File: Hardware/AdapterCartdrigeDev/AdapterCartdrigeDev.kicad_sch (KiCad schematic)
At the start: 3 parts, among them J1 ROM, U1 28C256

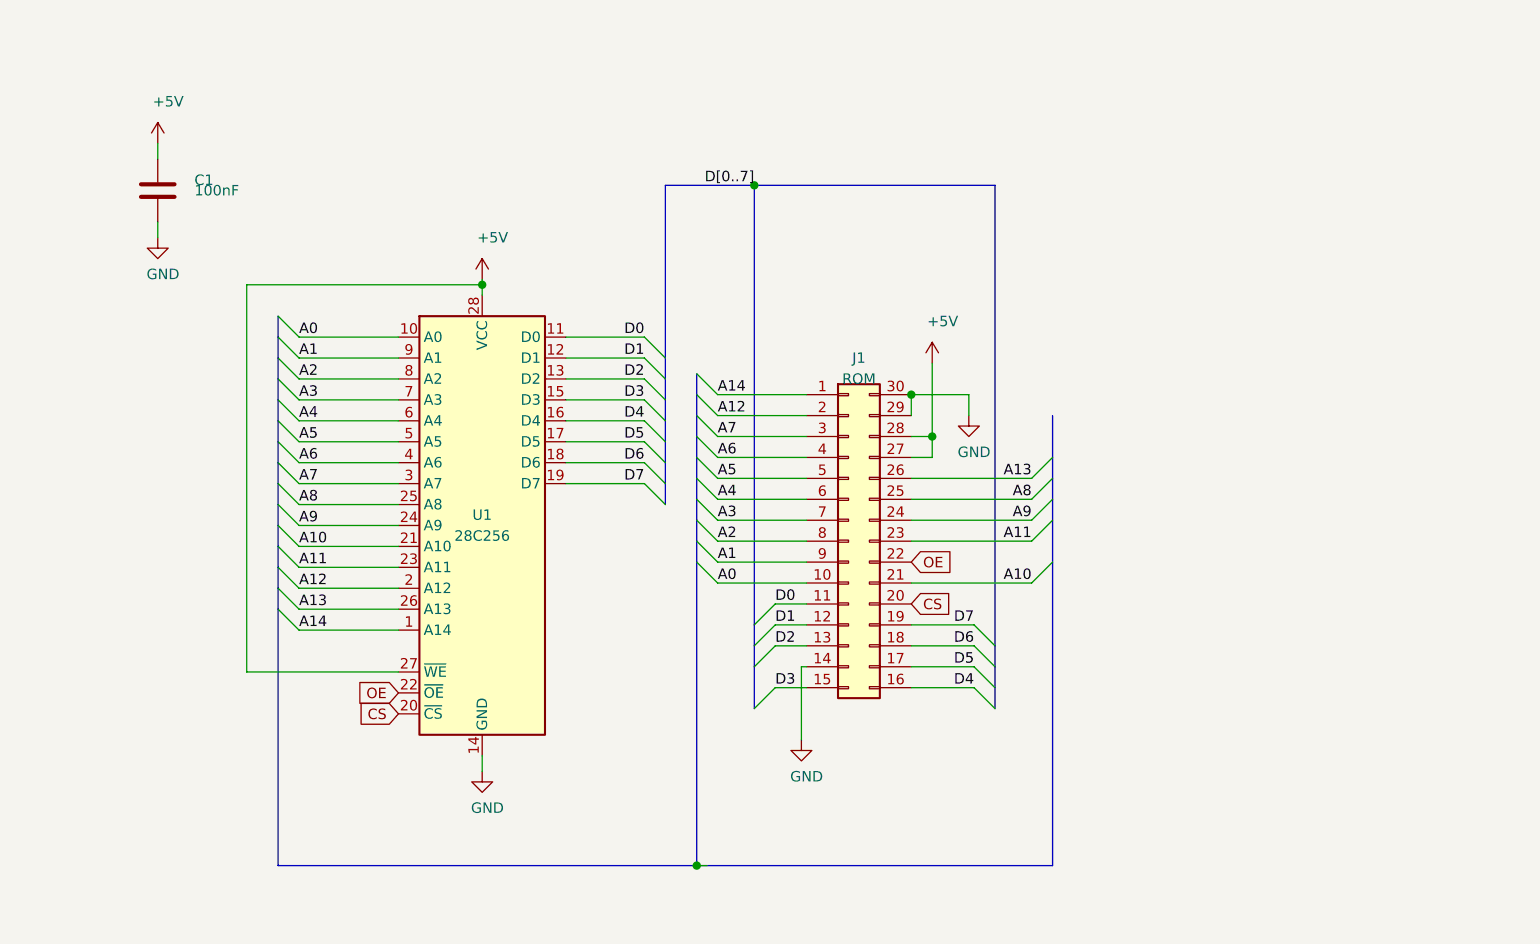
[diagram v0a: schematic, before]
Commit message: New PLD logic, VGA, DMA ...
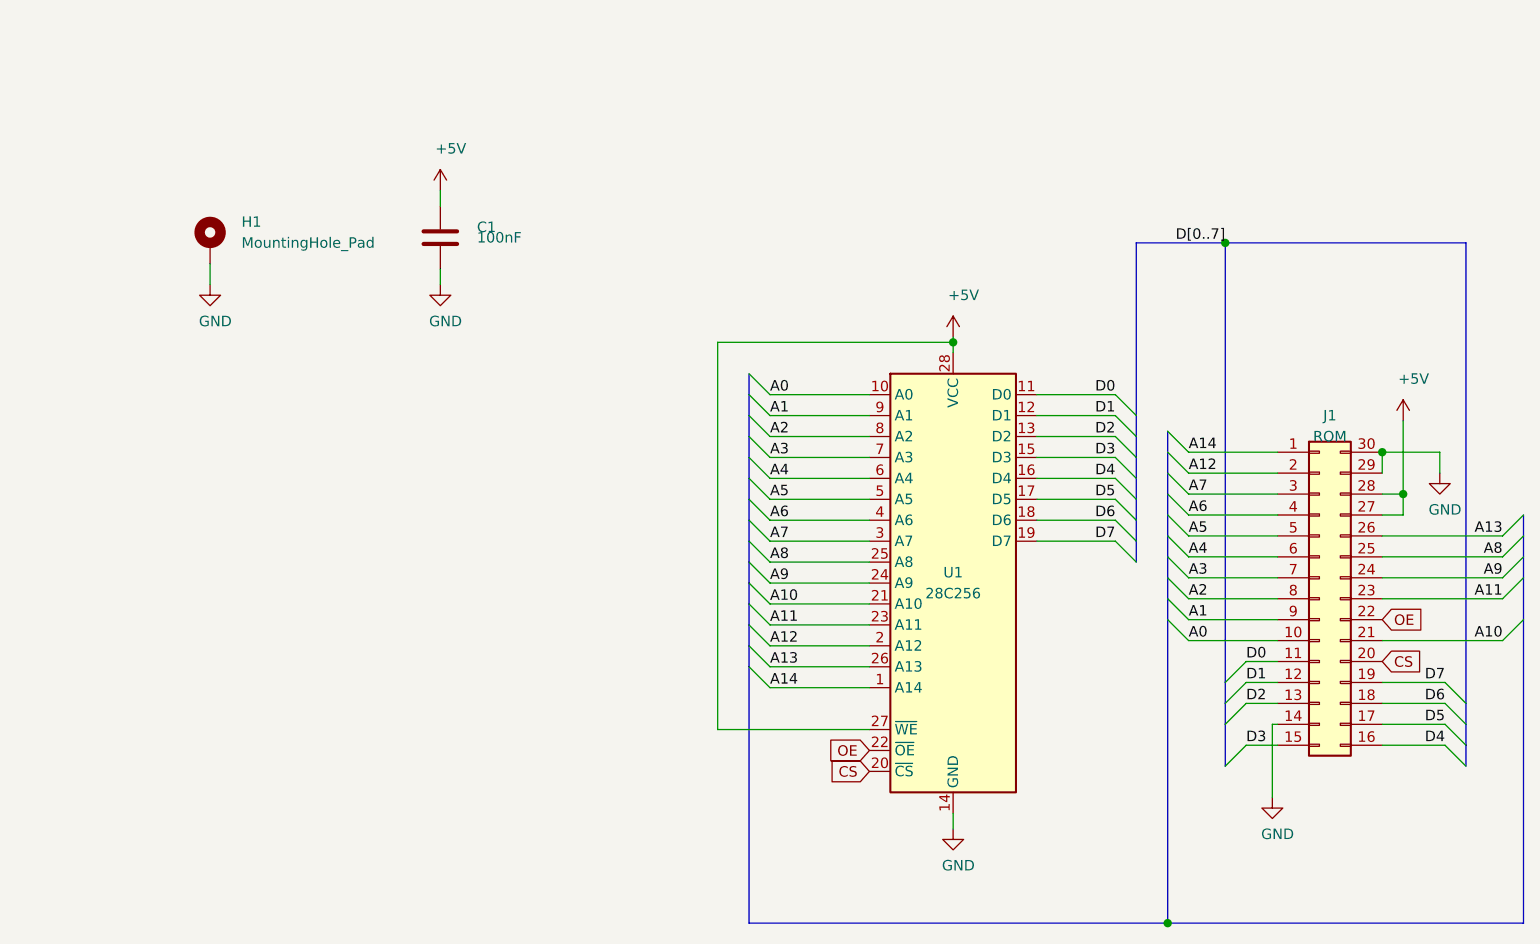
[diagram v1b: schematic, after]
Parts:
- added H1: MountingHole_Pad, MountingHole:MountingHole_3.2mm_M3, symbol Mechanical:MountingHole_Pad
- J1: footprint Connector_PinHeader_2.54mm:PinHeader_2x15_P2.54mm_Horizontal -> Connector_PinHeader_2.54mm:PinHeader_2x15_P2.54mm_Vertical
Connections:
- net GND: now also H1.1
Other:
- moved on the sheet: C1, J1, U1

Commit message: Fix
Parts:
- added H2, H3: MountingHole_Pad, MountingHole:MountingHole_3.2mm_M3, symbol Mechanical:MountingHole_Pad
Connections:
- net GND: now also H2.1, H3.1
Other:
- moved on the sheet: C1, H1, J1, U1
